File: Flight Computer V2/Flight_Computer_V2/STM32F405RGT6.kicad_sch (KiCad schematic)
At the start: 40 parts, among them J1 USB_B_Micro, J3 Conn_02x05_Odd_Even, SW1 SW_SPDT, U1 STM32F405RGTx, U2 AMS1117-3.3

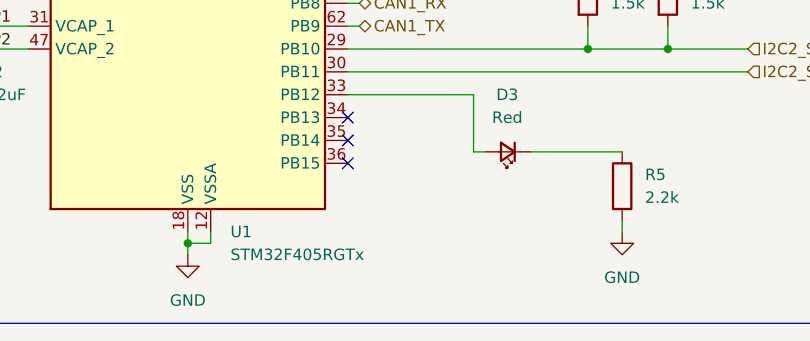
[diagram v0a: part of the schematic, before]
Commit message: added more sensors to flight computer v2
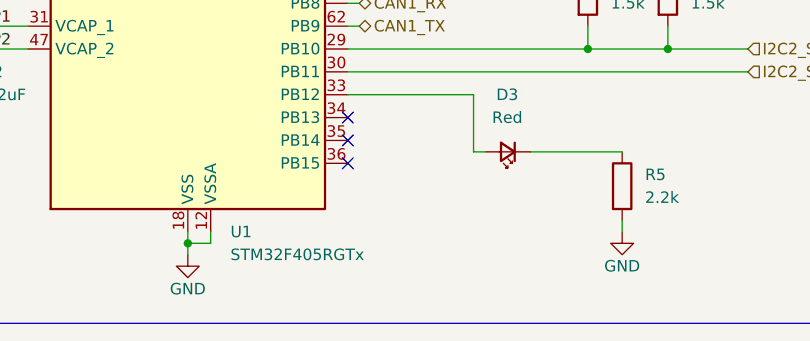
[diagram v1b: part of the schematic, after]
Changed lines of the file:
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@@
   )
   (symbol (lib_id "power:GND") (at 191.77 153.67 0) (unit 1)
-    (in_bom yes) (on_board yes) (dnp no) (fields_autoplaced)
+    (in_bom yes) (on_board yes) (dnp no)
     (property "Reference" "#PWR03" (at 191.77 160.02 0)
       (effects (font (size 1.27 1.27)) hide)
     )
-    (property "Value" "GND" (at 191.77 158.75 0)
+    (property "Value" "GND" (at 191.77 157.48 0)
       (effects (font (size 1.27 1.27)))
     )
@@
   )
   (symbol (lib_id "power:GND") (at 240.03 151.13 0) (unit 1)
-    (in_bom yes) (on_board yes) (dnp no) (fields_autoplaced)
+    (in_bom yes) (on_board yes) (dnp no)
     (property "Reference" "#PWR09" (at 240.03 157.48 0)
       (effects (font (size 1.27 1.27)) hide)
     )
-    (property "Value" "GND" (at 240.03 156.21 0)
-      (effects (font (size 1.27 1.27)))
-    )
+    (property "Value" "GND" (at 240.03 154.94 0)
+      (effects (font (size 1.27 1.27)))
+    )

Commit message: more flgiht computer v2 updates
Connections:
- net I2C1_SCL: no longer R4.2, U1.59 (PB7)
- net I2C2_SCL: no longer R7.2
- net I2C2_SDA: now also R7.2
- net GPIO_OUTPUT2: now reaches U1.37 (PC6)
- net GPIO_OUTPUT1: now reaches U1.41 (PA8)
- new net I2C1_SDA: R4.2, U1.59 (PB7)
- no-connect marks 22 -> 20
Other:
- moved on the sheet: R3, R4

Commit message: finalized schematic, added datasheets, and pdf of schematic
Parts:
- removed C15, C16: 22u, symbol Device:C
- removed R6, R7: 1.5k, symbol Device:R
- removed U2: AMS1117-3.3, Package_TO_SOT_SMD:SOT-223-3_TabPin2, symbol Regulator_Linear:AMS1117-3.3
- added D7: B5819W, symbol Device:D_Schottky_Small
- added D8: RED, symbol Device:LED
- added F2: 500 mA, symbol Device:Fuse_Small
- added FB9: 100 @ 100 MHz, symbol Device:FerriteBead_Small
- added R30: 1.5k, symbol Device:R
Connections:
- net +3.3V: now also D2.2 (A), FB2.2
- net +5V: now also D7.2 (A), D8.2 (A), FB9.2
- net GND: now also R30.2
- net PWR_LED_K: now also D8.1 (K), R30.1
- net VBUS: no longer D2.2 (A)
- net I2C2_SCL: no longer names the net of U1.29 (PB10)
- net I2C2_SDA: no longer names the net of U1.30 (PB11)
- new net: F2.2, FB9.1
- new net: D7.1 (K), F2.1
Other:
- note added: "Circuit Protection"
- note removed: "Input Voltage Regulator"
- company: (none) -> By: Dylan Haussecker
- title: (none) -> Avionics Flight Computer
- moved on the sheet: C12, C13, H1, H2, H3, H4, HSE1

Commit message: updated pcb
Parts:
- C1, C2, C3, C4, C5, C6, C7, C8: footprint Capacitor_SMD:C_0402_1005Metric -> Capacitor_SMD:C_1206_3216Metric
- C1, C2: footprint (none) -> Capacitor_SMD:C_0603_1608Metric
- C15: footprint Capacitor_SMD:C_0402_1005Metric -> Capacitor_SMD:C_0603_1608Metric
- D1, D3: footprint (none) -> LED_SMD:LED_0603_1608Metric
- D2, D7: footprint (none) -> Diode_SMD:D_SOD-123
- D8: footprint (none) -> LED_SMD:LED_0201_0603Metric
- F1: footprint (none) -> Fuse:Fuse_0805_2012Metric_Pad1.15x1.40mm_HandSolder
- F2: footprint (none) -> Fuse:Fuse_1206_3216Metric
- FB2, FB9: value 100 @ 100 MHz -> 600 @ 600 MHz; footprint (none) -> Inductor_SMD:L_0805_2012Metric
- FB3: footprint (none) -> Inductor_SMD:L_0805_2012Metric
- H1, H2, H3, H4: footprint (none) -> MountingHole:MountingHole_3.2mm_M3_ISO7380_Pad_TopBottom
- R1, R3, R4: footprint (none) -> Resistor_SMD:R_0402_1005Metric
- R2, R30, R5: footprint (none) -> Resistor_SMD:R_0603_1608Metric
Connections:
- net HSE_OUT is gone; now on net HSC_OUT: C13.1, HSE1.3
- net +3.3V: no longer D2.2 (A)
- net +5V: no longer D7.2 (A)
- net SWO: now also U1.55 (PB3)
- new net 3V3IN: D2.2 (A)
- new net 5VIN: D7.2 (A)
- no-connect marks 20 -> 21
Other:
- moved on the sheet: R3, R4

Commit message: updated v2 flight computer
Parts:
- removed C2, C8: 100u, Capacitor_SMD:C_1206_3216Metric, symbol Device:C_Small
- removed C9: 10u, Capacitor_SMD:C_0603_1608Metric, symbol Device:C_Small
- removed SW1: SW_SPDT, symbol Switch:SW_SPDT
- added JP3: ~, Jumper:SolderJumper-2_P1.3mm_Open_Pad1.0x1.5mm, symbol Jumper:SolderJumper_2_Open
- C1: value 100u -> 4u7
- C3, C4, C5, C6, C7: value 100u -> 100n; footprint Capacitor_SMD:C_1206_3216Metric -> Capacitor_SMD:C_0402_1005Metric
- J1: footprint (none) -> Connector_USB:USB_Micro-B_Molex-105017-0001
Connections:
- net SW_BOOT0 is gone; now on net GND: R1.1
- net +3.3V: now also JP3.1 (A)
- net BOOT0: now also JP3.2 (B)
- net GND: no longer C1.2, C3.2, C4.2, C5.2, C6.2, C7.2
- net PC13: now reaches U1.2 (PC13)
- net PB2: now reaches U1.28 (PB2)
- net PB10: now reaches U1.29 (PB10)
- net PC14: now reaches U1.3 (PC14)
- net PB11: now reaches U1.30 (PB11)
- net PB13: now reaches U1.34 (PB13)
- net PB14: now reaches U1.35 (PB14)
- net PB15: now reaches U1.36 (PB15)
- net PC7: now reaches U1.38 (PC7)
- net PC8: now reaches U1.39 (PC8)
- net PC15: now reaches U1.4 (PC15)
- net PC9: now reaches U1.40 (PC9)
- net PA15: now reaches U1.50 (PA15)
- net PC10: now reaches U1.51 (PC10)
- net PC11: now reaches U1.52 (PC11)
- net PB4: now reaches U1.56 (PB4)
- net PB5: now reaches U1.57 (PB5)
- new net: C1.2, C3.2, C4.2, C5.2, C6.2, C7.2
- no-connect marks 21 -> 4
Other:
- note added: "Decoupling Capacitors"
- note removed: "Decoupling Capacitors: 2x100u per VDD + 10u bulk close to chip"
- moved on the sheet: C3, C4, C5, C6, C7
